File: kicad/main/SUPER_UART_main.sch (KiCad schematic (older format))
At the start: 9 parts, among them SW1 74HC4053D, SW2 74HC4053D, U2 FT4232HL_UART, U4 74AHC1G125

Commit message: Working on schematic
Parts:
- removed C?: 100n, 0603_N, symbol C
- removed D1: BAS70-06, SOT23-3_N, symbol BAS70-06
- removed R1: 1k, 0603_R_N, symbol R_V
- removed unit 1 of SW1
- removed unit 2 of SW1
- removed unit 3 of SW1
- removed unit 1 of SW2
- removed unit 2 of SW2
- removed unit 3 of SW2
- removed U4: 74AHC1G125, symbol 74AHC1G125
- added C? (x3): 100n, 0603_N, symbol C
- added U? (x2): XC9536XL-10VQG44, Xilinx_VQFP44_N, symbol XC9536XL-10VQG44
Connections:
- net +3V3: now also C?.1, C?.1, C?.1, U?.15 (VCCINT), U?.26 (VCCIO), U?.35 (VCCINT)
- net GND: now also C?.2, C?.2, C?.2, U?.17 (GND), U?.25 (GND), U?.4 (GND)

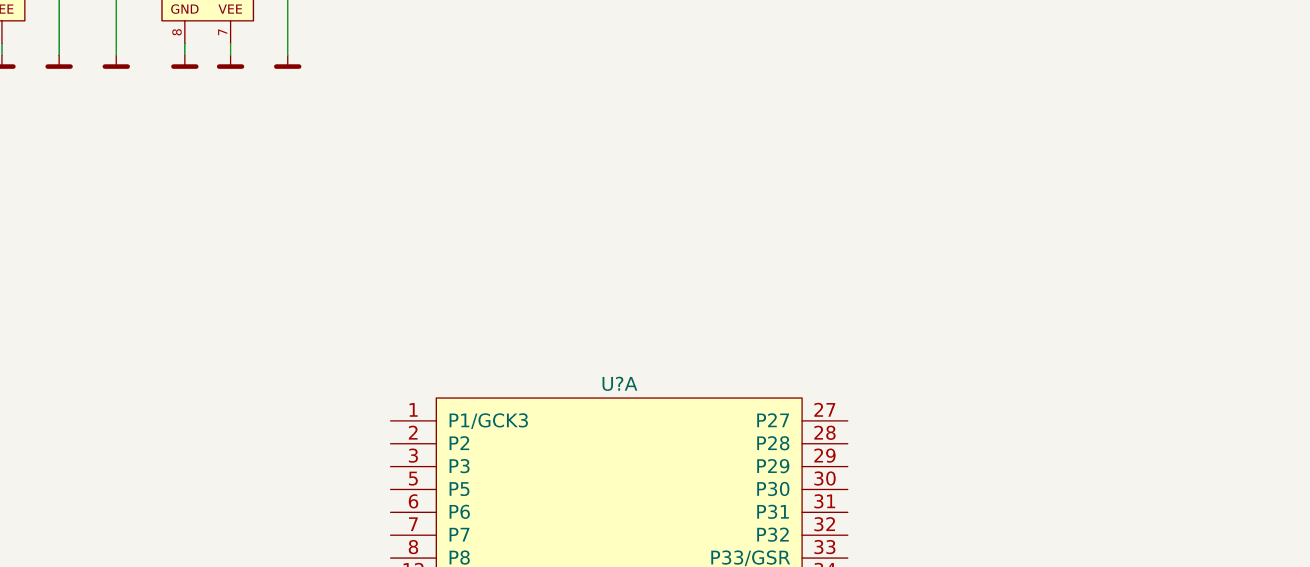
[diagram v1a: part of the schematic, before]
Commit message: Routing before moving to 4 layers
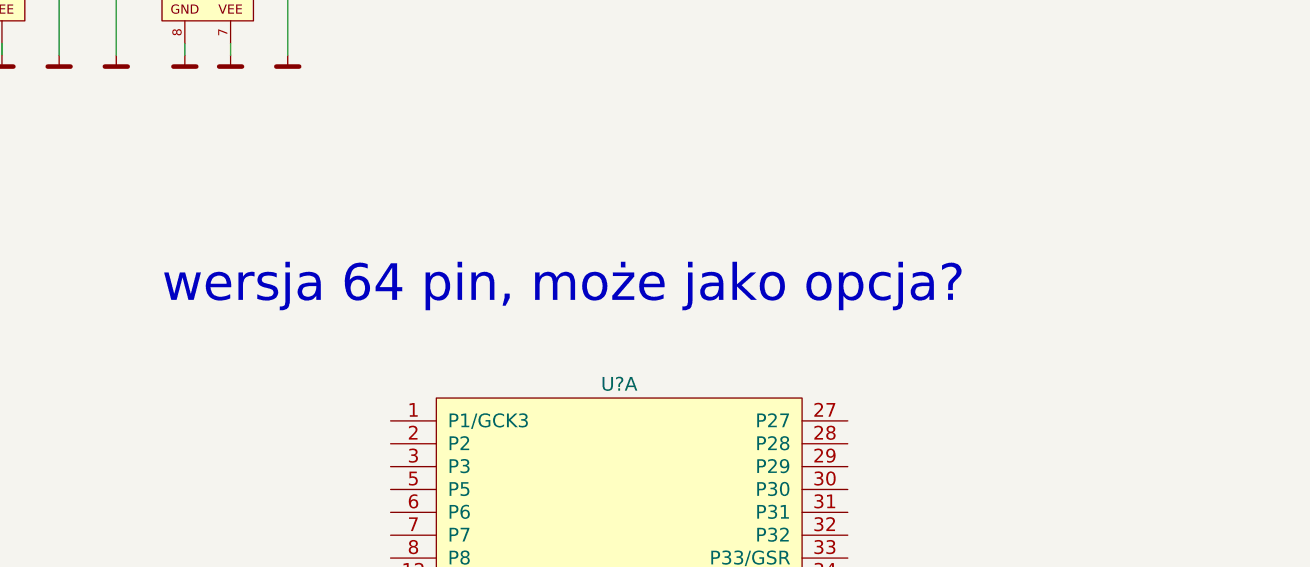
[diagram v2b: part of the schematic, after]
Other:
- note added: "wersja 64 pin, może jako opcja?"
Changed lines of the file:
@@
 	11050 7550 11050 7500
 Connection ~ 11050 7500
+Text Notes 10600 4100 0    160  ~ 0
+wersja 64 pin, może jako opcja?
 $EndSCHEMATC

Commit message: Add missing files
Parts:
- removed C? (x2): 100n, 0603_N, symbol C
- removed SW1, SW2: 74HC4053D, niceSemiconductors:SOIC-16_N, symbol 74HC4053D
- removed U? (x2): XC9536XL-10VQG44, Xilinx_VQFP44_N, symbol XC9536XL-10VQG44
- added C1, C21, C24, C29, C8, C9: 10u, niceRLC:0805_N, symbol C
- added C10, C11, C12, C13, C14, C15, C16, C17, C18, C19, C2, C20, C25, C3, C4, C5: 100n, 0603_N, symbol C
- added C22, C23: 1u, 0603_N, symbol C
- added C6, C7: 22p, 0603_N, symbol C
- added CON1: PIN-2x4, nicePinheaders:PIN-2x4_F_angled_N, symbol PIN-2x4
- added CON2: PIN-2x2, nicePinheaders:PIN-2x2_F_angled_N, symbol PIN-2x2
- added CON3: PIN-2x5, nicePinheaders:PIN-2x5_F_angled_N, symbol PIN-2x5
- added CON4: PIN-2x12, nicePinheaders:PIN-2x12_F_angled_N, symbol PIN-2x12
- added CON5: JTAG, PIN-1x6_N, symbol PIN-1x6
- added D1, D2: BAS70, SOT23-3_N, symbol BAS70
- added J1: USB_B, Connectors:USB_B, symbol USB_B
- added MECH1: case, dummy, symbol dummy_mech
- added MECH2: case, pnMechanical:frog, symbol dummy_mech
- added Q1: 12MHz, XT3.2x2.5_N, symbol XT_3.2x2.5
- added R1, R2, R3, R4: 24R, 0603_R_N, symbol R
- added R10, R15, R8, R9: 10k, 0603_R_N, symbol R_V
- added R11: 2k2, 0603_R_N, symbol R
- added R12, R13, R14: 10k, 0603_R_N, symbol R
- added R5: 12k, 0603_R_N, symbol R
- added R6, R7: FERR, 0603_R_N, symbol R
- added REL1: V23026, pnRelay:V23026, symbol Relay_SPDT
- added T1, T2: N-MOS_small, SOT23-3_N, symbol N-MOS_small
- added TP1, TP2, TP3, TP4, TP5: Testpoint, pnConnector:TP_1mm, symbol Testpoint
- added U1: ADuM3160, SOIC-16_N, symbol ADuM3160
- added U3: USBLC6-2SC6, SOT23-6_N, symbol USBLC6-2SC6
- added U4: AM1S-0505SZ, AM1S-Z_N, symbol AM1S-0505SZ
- added U5: MIC5504-3.3YM5-TR, niceSemiconductors:SOT23-5_N, symbol MIC5504-3.3YM5-TR
- added U6: 93LC46BT-I/OT, niceSemiconductors:SOT23-6_N, symbol 93LC46BT-I/OT
- added U7: XC9536XL-10VQG64, Xilinx_VQFP64_M, symbol XC9536XL-10VQG64
- added X1: BUZZER, pnOther:buzzer_12x9.0, symbol PIN-1x2
- U2: footprint FTDI_LQFP64_N -> FTDI_LQFP64_M; Fieldname (none) -> Value
- gave numbers to parts that had none: 3
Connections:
- net labels added: +1V8, +5V, AUX1, AUX2, AUX3, BUZZER, CPLD_BOOT_EN, CPLD_OE, CTS_A, CTS_B, CTS_C, CTS_D, D+, D-, DCD_D, DSR_D, DTR_A, DTR_B, DTR_C, DTR_D, EECLK, EECS, EEDATA, FTDI_RESET, ISO_D+, ISO_D-, ISO_GND, ISO_VDD, OPTO_EN, RI_D, RTS_D, RXD_A, RXD_B, RXD_C, RXD_D, SR_CLK, SR_DATA, SR_LOAD, TCK, TDI, TDO, TMS, TXD_A, TXD_B, TXD_C, TXD_D, VPHY, VPLL, ~CTS_A_OC, ~CTS_B_OC, ~PWREN, ~RXD_A_OC, ~RXD_B_OC, ~USB_SUSPEND
- net labels removed: FTDI_CTS_C, FTDI_CTS_D, FTDI_DCD_A, FTDI_DSR_A, FTDI_DTR_C, FTDI_DTR_D, FTDI_RI_A, FTDI_TXD_C
- wire segments 49 -> 414
- no-connect marks 0 -> 18
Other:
- note added: "&"
- note added: "CS"
- note added: "CTS"
- note added: "DTR"
- note added: "FTDI PIN\n\nRxD\nTxD\nCTS\nRTS"
- note added: "FTDI PIN\n\nRxD\nTxD\nRTS"
- note added: "Function\n\nMOSI\nSCK\nCS\nMISO"
- note added: "Function\n\nSDA_OUT\nSCL\nSDA_IN"
- note added: "I2C connections"
- note added: "I2C mode"
- note added: "MISO"
- note added: "MOSI"
- note added: "Opto channel\n\nDTR\nTxD\nCTS"
- note added: "Opto channel\n\nDTR\nTxD\nRTS\nCTS"
- note added: "Output pin\n\nCTS\nTxD\nCTS"
- note added: "Output pin\n\nRxD\nTxD\nRTS\nCTS"
- note added: "RTS"
- note added: "RxD"
- note added: "RxD B\n\nTxD B"
- note added: "RxD C\n\nTxD C"
- note added: "RxD D"
- note added: "RxD D\n\nTxD D"
- note added: "SCK"
- note added: "SCL"
- note added: "SDA"
- note added: "SPI connections"
- note added: "SPI mode"
- note added: "SPY mode"
- note added: "TxD"
- note added: "TxD B"
- note added: "TxD C"
- note added: "TxD D"
- note added: "UART mode"
- note added: "WP"
- note added: "normal mode"
- note removed: "wersja 64 pin, może jako opcja?"
- moved on the sheet: C26, C27, C28, U2
